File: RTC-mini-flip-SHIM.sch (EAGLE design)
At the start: 9 parts, among them IC1 DS3231/SO

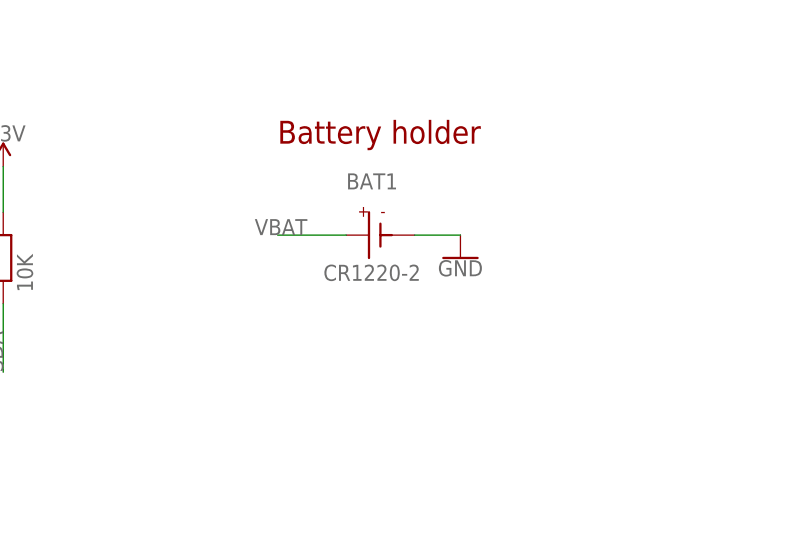
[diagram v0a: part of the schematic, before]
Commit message: Added battery connector. Generated CAM.
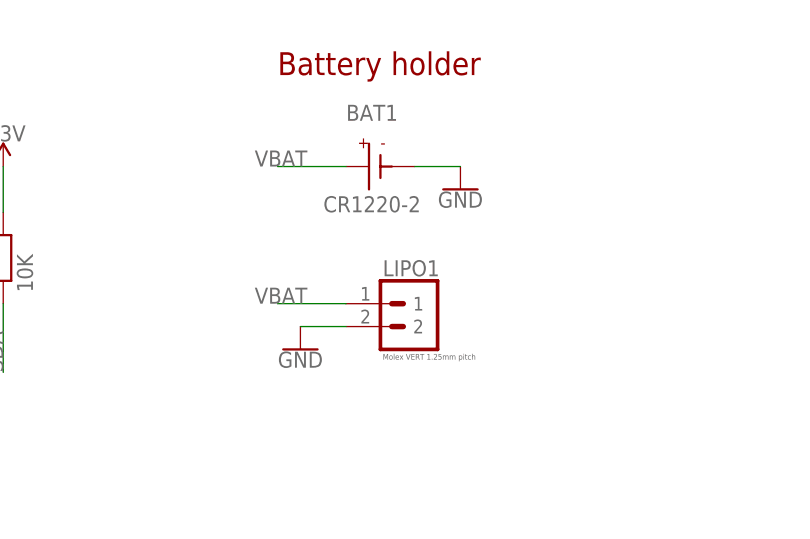
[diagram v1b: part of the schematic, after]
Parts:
- added LIPO1: Molex VERT 1.25mm pitch, PiB_connectors:1X02_MOLEX_0530470210_VERT-MALE_PITCH-1.25MM
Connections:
- net GND: now also LIPO1.2
- net VBAT: now also LIPO1.1
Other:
- moved on the sheet: BAT1
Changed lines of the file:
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@@
 <layer number="154" name="FabDoc2" color="2" fill="1" visible="no" active="no"/>
 <layer number="155" name="FabDoc3" color="7" fill="15" visible="no" active="no"/>
+<layer number="160" name="tMountFaceplate" color="7" fill="1" visible="yes" active="yes"/>
+<layer number="161" name="bMountFaceplate" color="7" fill="1" visible="yes" active="yes"/>
+<layer number="162" name="tCopperArt" color="7" fill="1" visible="yes" active="yes"/>
+<layer number="163" name="bCopperArt" color="7" fill="1" visible="yes" active="yes"/>
+<layer number="164" name="tRubout" color="7" fill="1" visible="yes" active="yes"/>
+<layer number="165" name="bRubout" color="7" fill="1" visible="yes" active="yes"/>
+<layer number="167" name="Fiducials" color="7" fill="1" visible="yes" active="yes"/>
+<layer number="169" name="internal" color="7" fill="1" visible="yes" active="yes"/>
 <layer number="199" name="Contour" color="7" fill="1" visible="no" active="yes"/>
 <layer number="200" name="200bmp" color="1" fill="10" visible="no" active="yes"/>
@@
 <part name="GND9" library="SparkFun-PowerSymbols" library_urn="urn:adsk.eagle:library:530" deviceset="GND" device=""/>
 <part name="LOGO1" library="_my_logos" deviceset="MFDECLOGO" device="_L_10MM"/>
+<part name="LIPO1" library="PiB_connectors" deviceset="1X02_MOLEX" device="_0530470210_VERT-MALE_PITCH-1.25MM" package3d_urn="urn:adsk.eagle:package:2973718/3" value="Molex VERT 1.25mm pitch"/>
+<part name="GND11" library="SparkFun-PowerSymbols" library_urn="urn:adsk.eagle:library:530" deviceset="GND" device=""/>
 </parts>
 <sheets>
@@
 <text x="152.4" y="124.46" size="2.54" layer="94">Caps and pullups</text>
 <text x="104.14" y="124.46" size="2.54" layer="94">Mini connector</text>
-<text x="210.82" y="116.84" size="2.54" layer="94">Battery holder</text>
+<text x="210.82" y="124.46" size="2.54" layer="94">Battery holder</text>
 </plain>
 <instances>
@@
 <attribute name="VALUE" x="101.6" y="93.726" size="1.778" layer="96" align="top-center"/>
 </instance>
-<instance part="BAT1" gate="G$1" x="220.98" y="106.68" smashed="yes">
-<attribute name="NAME" x="218.44" y="111.76" size="1.778" layer="96"/>
-<attribute name="VALUE" x="215.9" y="101.6" size="1.778" layer="96"/>
-</instance>
-<instance part="GND9" gate="1" x="231.14" y="104.14" smashed="yes">
-<attribute name="VALUE" x="231.14" y="103.886" size="1.778" layer="96" align="top-center"/>
+<instance part="BAT1" gate="G$1" x="220.98" y="114.3" smashed="yes">
+<attribute name="NAME" x="218.44" y="119.38" size="1.778" layer="96"/>
+<attribute name="VALUE" x="215.9" y="109.22" size="1.778" layer="96"/>
+</instance>
+<instance part="GND9" gate="1" x="231.14" y="111.76" smashed="yes">
+<attribute name="VALUE" x="231.14" y="111.506" size="1.778" layer="96" align="top-center"/>
 </instance>
 <instance part="LOGO1" gate="G$1" x="134.62" y="2.54" smashed="yes"/>
+<instance part="LIPO1" gate="G$1" x="226.06" y="99.06" smashed="yes" rot="MR0">
+<attribute name="VALUE" x="222.504" y="93.472" size="0.635" layer="96" font="vector" ratio="10" rot="MR0" align="top-right"/>
+<attribute name="NAME" x="222.504" y="102.108" size="1.778" layer="95" ratio="10" rot="MR0" align="bottom-right"/>
+</instance>
+<instance part="GND11" gate="1" x="213.36" y="93.98" smashed="yes">
+<attribute name="VALUE" x="213.36" y="93.726" size="1.778" layer="96" align="top-center"/>
+</instance>
 </instances>
 <busses>
@@
 <segment>
 <pinref part="BAT1" gate="G$1" pin="BAT+"/>
-<wire x1="218.44" y1="106.68" x2="210.82" y2="106.68" width="0.1524" layer="91"/>
-<label x="208.28" y="106.68" size="1.778" layer="95"/>
+<wire x1="218.44" y1="114.3" x2="210.82" y2="114.3" width="0.1524" layer="91"/>
+<label x="208.28" y="114.3" size="1.778" layer="95"/>
+</segment>
+<segment>
+<pinref part="LIPO1" gate="G$1" pin="1"/>
+<wire x1="218.44" y1="99.06" x2="210.82" y2="99.06" width="0.1524" layer="91"/>
+<label x="208.28" y="99.06" size="1.778" layer="95"/>
 </segment>
 </net>
@@
 <segment>
 <pinref part="BAT1" gate="G$1" pin="BAT-"/>
-<wire x1="226.06" y1="106.68" x2="231.14" y2="106.68" width="0.1524" layer="91"/>
+<wire x1="226.06" y1="114.3" x2="231.14" y2="114.3" width="0.1524" layer="91"/>
 <pinref part="GND9" gate="1" pin="GND"/>
 </segment>
-</net>
+<segment>
+<pinref part="LIPO1" gate="G$1" pin="2"/>
+<wire x1="218.44" y1="96.52" x2="213.36" y2="96.52" width="0.1524" layer="91"/>
+<pinref part="GND11" gate="1" pin="GND"/>
+</segment>
+</net>

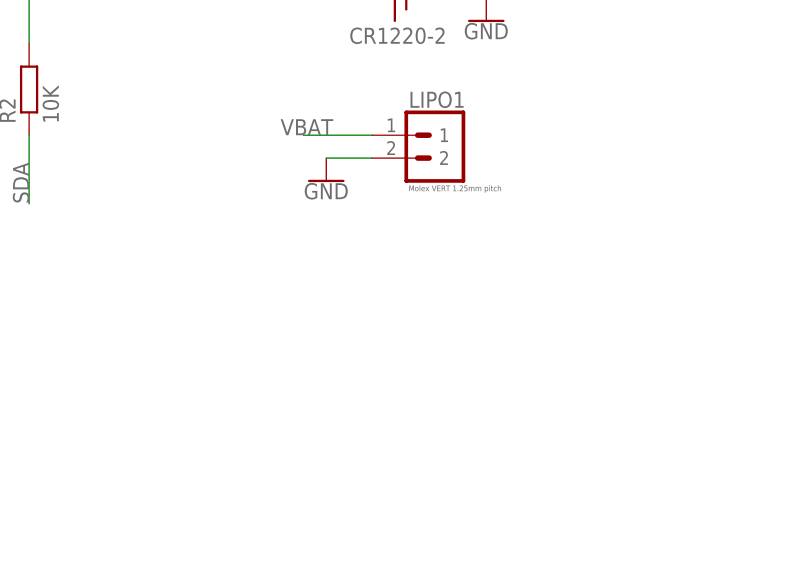
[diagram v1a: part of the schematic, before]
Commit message: Add battery connector to the front of mini SHIM too. Generate new CAM.
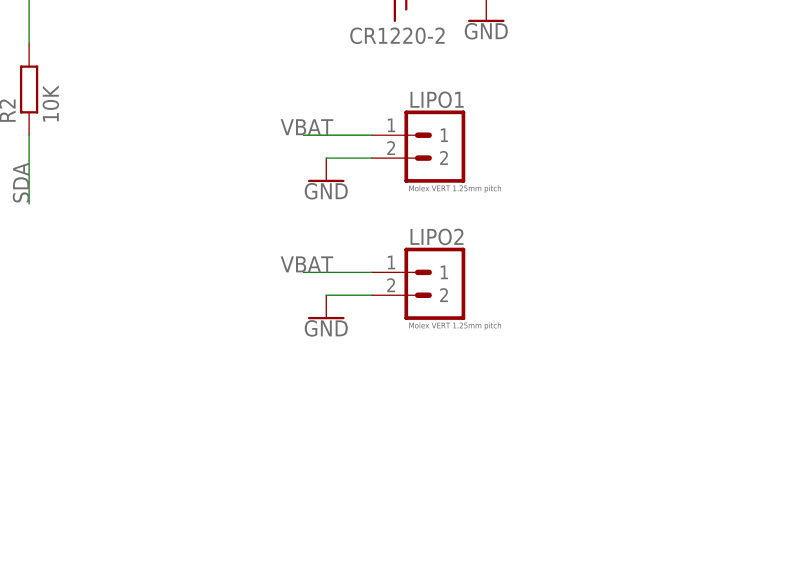
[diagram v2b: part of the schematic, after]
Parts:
- added LIPO2: Molex VERT 1.25mm pitch, PiB_connectors:1X02_MOLEX_0530470210_VERT-MALE_PITCH-1.25MM
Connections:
- net GND: now also LIPO2.2
- net VBAT: now also LIPO2.1
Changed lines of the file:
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@@
 <part name="LIPO1" library="PiB_connectors" deviceset="1X02_MOLEX" device="_0530470210_VERT-MALE_PITCH-1.25MM" package3d_urn="urn:adsk.eagle:package:2973718/3" value="Molex VERT 1.25mm pitch"/>
 <part name="GND11" library="SparkFun-PowerSymbols" library_urn="urn:adsk.eagle:library:530" deviceset="GND" device=""/>
+<part name="LIPO2" library="PiB_connectors" deviceset="1X02_MOLEX" device="_0530470210_VERT-MALE_PITCH-1.25MM" package3d_urn="urn:adsk.eagle:package:2973718/3" value="Molex VERT 1.25mm pitch"/>
+<part name="GND6" library="SparkFun-PowerSymbols" library_urn="urn:adsk.eagle:library:530" deviceset="GND" device=""/>
 </parts>
 <sheets>
@@
 <attribute name="VALUE" x="213.36" y="93.726" size="1.778" layer="96" align="top-center"/>
 </instance>
+<instance part="LIPO2" gate="G$1" x="226.06" y="83.82" smashed="yes" rot="MR0">
+<attribute name="VALUE" x="222.504" y="78.232" size="0.635" layer="96" font="vector" ratio="10" rot="MR0" align="top-right"/>
+<attribute name="NAME" x="222.504" y="86.868" size="1.778" layer="95" ratio="10" rot="MR0" align="bottom-right"/>
+</instance>
+<instance part="GND6" gate="1" x="213.36" y="78.74" smashed="yes">
+<attribute name="VALUE" x="213.36" y="78.486" size="1.778" layer="96" align="top-center"/>
+</instance>
 </instances>
 <busses>
@@
 <wire x1="218.44" y1="99.06" x2="210.82" y2="99.06" width="0.1524" layer="91"/>
 <label x="208.28" y="99.06" size="1.778" layer="95"/>
+</segment>
+<segment>
+<pinref part="LIPO2" gate="G$1" pin="1"/>
+<wire x1="218.44" y1="83.82" x2="210.82" y2="83.82" width="0.1524" layer="91"/>
+<label x="208.28" y="83.82" size="1.778" layer="95"/>
 </segment>
 </net>
@@
 <pinref part="GND11" gate="1" pin="GND"/>
 </segment>
-</net>
+<segment>
+<pinref part="LIPO2" gate="G$1" pin="2"/>
+<wire x1="218.44" y1="81.28" x2="213.36" y2="81.28" width="0.1524" layer="91"/>
+<pinref part="GND6" gate="1" pin="GND"/>
+</segment>
+</net>

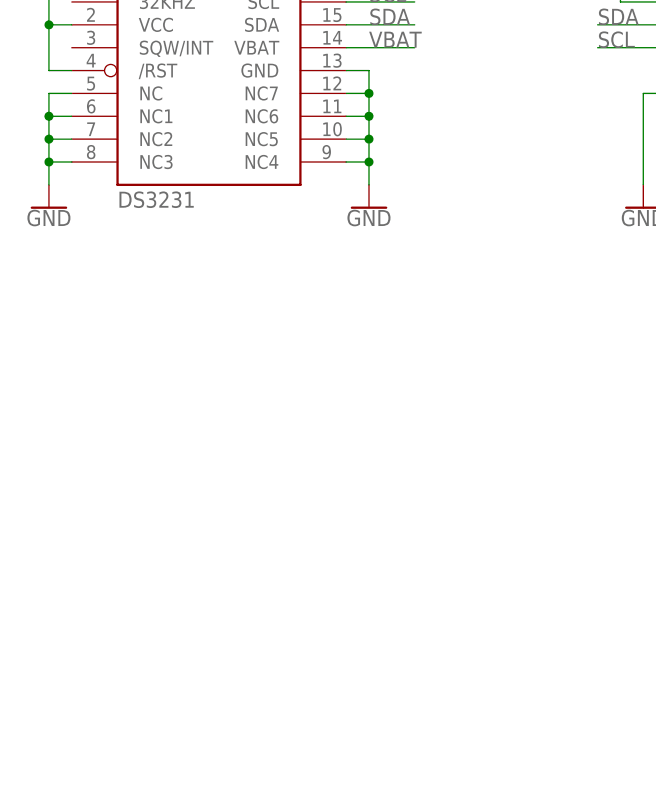
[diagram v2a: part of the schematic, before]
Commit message: Moved some stuff around. Add second footprint. Moved battery away from center for better flipability.
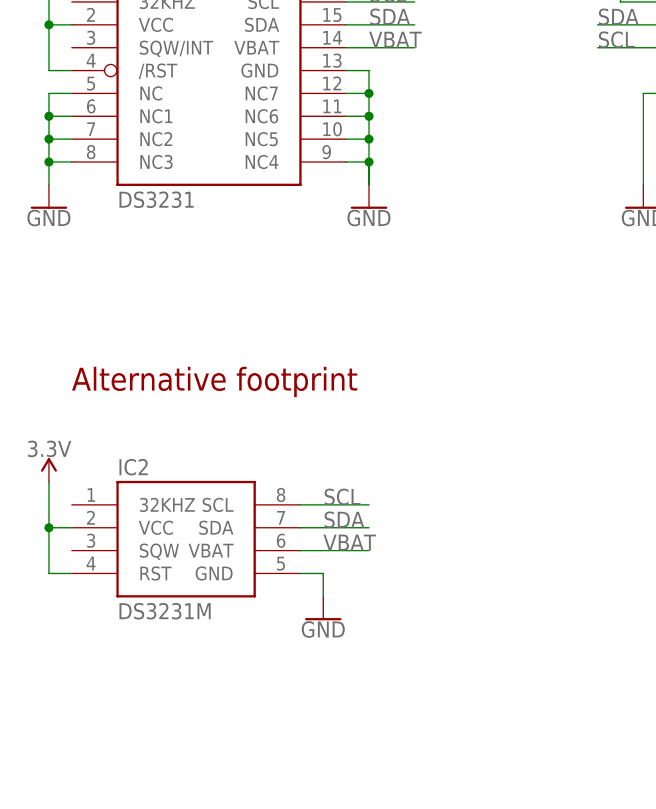
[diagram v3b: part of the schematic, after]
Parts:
- added IC2: DS3231M, SparkFun-Clocks:DS3231M
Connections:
- net 3.3V: now also IC2.RST, IC2.VCC
- net GND: now also IC2.GND
- net SCL: now also IC2.SCL
- net SDA: now also IC2.SDA
- net VBAT: now also IC2.VBAT
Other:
- note added: "Alternative footprint"
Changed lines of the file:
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@@
 <part name="LIPO2" library="PiB_connectors" deviceset="1X02_MOLEX" device="_0530470210_VERT-MALE_PITCH-1.25MM" package3d_urn="urn:adsk.eagle:package:2973718/3" value="Molex VERT 1.25mm pitch"/>
 <part name="GND6" library="SparkFun-PowerSymbols" library_urn="urn:adsk.eagle:library:530" deviceset="GND" device=""/>
+<part name="IC2" library="SparkFun-Clocks" library_urn="urn:adsk.eagle:library:511" deviceset="DS3231M" device="" package3d_urn="urn:adsk.eagle:package:37530/1"/>
+<part name="SUPPLY7" library="SparkFun-PowerSymbols" library_urn="urn:adsk.eagle:library:530" deviceset="3.3V" device=""/>
+<part name="GND7" library="SparkFun-PowerSymbols" library_urn="urn:adsk.eagle:library:530" deviceset="GND" device=""/>
 </parts>
 <sheets>
@@
 <text x="104.14" y="124.46" size="2.54" layer="94">Mini connector</text>
 <text x="210.82" y="124.46" size="2.54" layer="94">Battery holder</text>
+<text x="38.1" y="73.66" size="2.54" layer="94">Alternative footprint</text>
 </plain>
 <instances>
@@
 <attribute name="VALUE" x="213.36" y="78.486" size="1.778" layer="96" align="top-center"/>
 </instance>
+<instance part="IC2" gate="G$1" x="50.8" y="55.88" smashed="yes">
+<attribute name="NAME" x="43.18" y="64.262" size="1.778" layer="95" ratio="10"/>
+<attribute name="VALUE" x="43.18" y="48.26" size="1.778" layer="96" ratio="10"/>
+</instance>
+<instance part="SUPPLY7" gate="G$1" x="35.56" y="63.5" smashed="yes">
+<attribute name="VALUE" x="35.56" y="66.294" size="1.778" layer="96" align="bottom-center"/>
+</instance>
+<instance part="GND7" gate="1" x="66.04" y="48.26" smashed="yes">
+<attribute name="VALUE" x="66.04" y="48.006" size="1.778" layer="96" align="top-center"/>
+</instance>
 </instances>
 <busses>
@@
 <label x="208.28" y="83.82" size="1.778" layer="95"/>
 </segment>
+<segment>
+<pinref part="IC2" gate="G$1" pin="VBAT"/>
+<wire x1="63.5" y1="55.88" x2="71.12" y2="55.88" width="0.1524" layer="91"/>
+<label x="66.04" y="55.88" size="1.778" layer="95"/>
+</segment>
 </net>
 <net name="SCL" class="0">
@@
 <label x="96.52" y="111.76" size="1.778" layer="95"/>
 </segment>
+<segment>
+<pinref part="IC2" gate="G$1" pin="SCL"/>
+<wire x1="63.5" y1="60.96" x2="71.12" y2="60.96" width="0.1524" layer="91"/>
+<label x="66.04" y="60.96" size="1.778" layer="95"/>
+</segment>
 </net>
 <net name="SDA" class="0">
@@
 <wire x1="104.14" y1="114.3" x2="96.52" y2="114.3" width="0.1524" layer="91"/>
 <label x="96.52" y="114.3" size="1.778" layer="95"/>
+</segment>
+<segment>
+<pinref part="IC2" gate="G$1" pin="SDA"/>
+<wire x1="63.5" y1="58.42" x2="71.12" y2="58.42" width="0.1524" layer="91"/>
+<label x="66.04" y="58.42" size="1.778" layer="95"/>
 </segment>
 </net>
@@
 <wire x1="99.06" y1="116.84" x2="99.06" y2="119.38" width="0.1524" layer="91"/>
 <pinref part="SUPPLY6" gate="G$1" pin="3.3V"/>
+</segment>
+<segment>
+<pinref part="IC2" gate="G$1" pin="RST"/>
+<wire x1="38.1" y1="53.34" x2="35.56" y2="53.34" width="0.1524" layer="91"/>
+<wire x1="35.56" y1="53.34" x2="35.56" y2="58.42" width="0.1524" layer="91"/>
+<pinref part="IC2" gate="G$1" pin="VCC"/>
+<wire x1="35.56" y1="58.42" x2="35.56" y2="63.5" width="0.1524" layer="91"/>
+<wire x1="38.1" y1="58.42" x2="35.56" y2="58.42" width="0.1524" layer="91"/>
+<junction x="35.56" y="58.42"/>
+<pinref part="SUPPLY7" gate="G$1" pin="3.3V"/>
 </segment>
 </net>
@@
 <wire x1="68.58" y1="106.68" x2="71.12" y2="106.68" width="0.1524" layer="91"/>
 <junction x="71.12" y="106.68"/>
+<wire x1="71.12" y1="99.06" x2="71.12" y2="96.52" width="0.1524" layer="91"/>
 </segment>
 <segment>
@@
 <pinref part="GND6" gate="1" pin="GND"/>
 </segment>
-</net>
+<segment>
+<pinref part="IC2" gate="G$1" pin="GND"/>
+<wire x1="63.5" y1="53.34" x2="66.04" y2="53.34" width="0.1524" layer="91"/>
+<wire x1="66.04" y1="53.34" x2="66.04" y2="50.8" width="0.1524" layer="91"/>
+<pinref part="GND7" gate="1" pin="GND"/>
+</segment>
+</net>

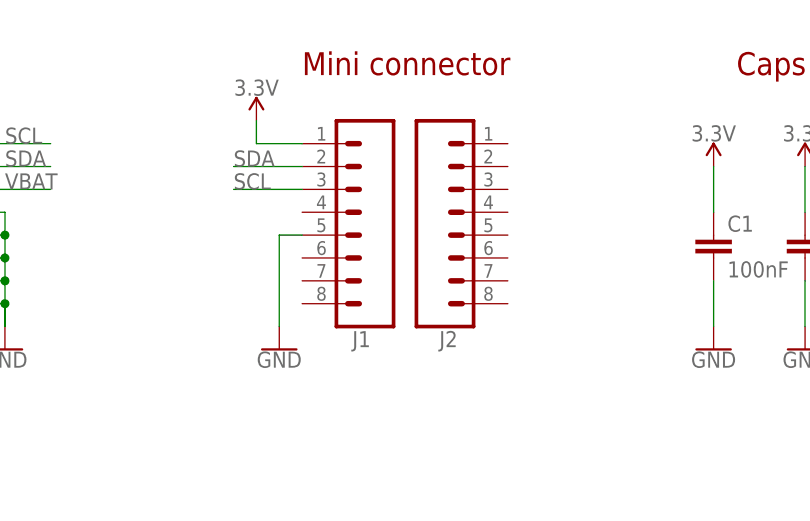
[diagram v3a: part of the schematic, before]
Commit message: Changed mini SHIM layout. Traced mini SHIM.
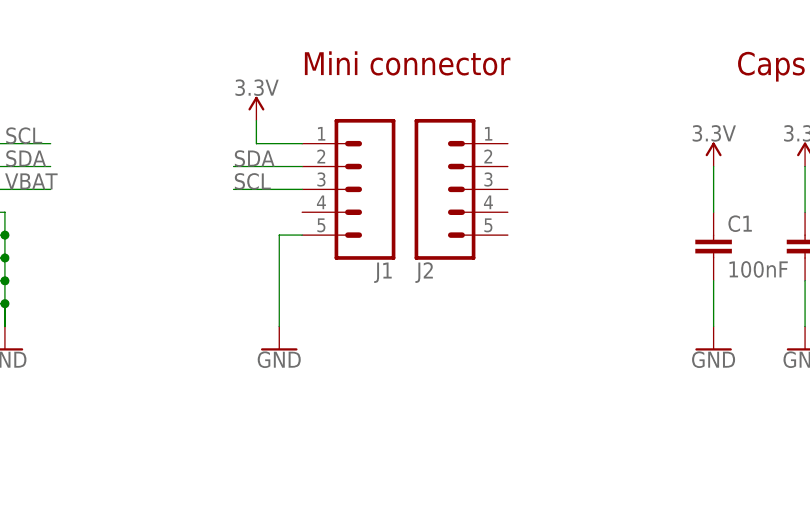
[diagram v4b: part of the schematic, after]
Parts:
- J1, J2: device SparkFun-Connectors:CONN_08LOCK_NO_SILK -> SparkFun-Connectors:CONN_05LOCK
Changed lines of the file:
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@@
 <part name="SUPPLY4" library="SparkFun-PowerSymbols" library_urn="urn:adsk.eagle:library:530" deviceset="3.3V" device=""/>
 <part name="SUPPLY5" library="SparkFun-PowerSymbols" library_urn="urn:adsk.eagle:library:530" deviceset="3.3V" device=""/>
-<part name="J1" library="SparkFun-Connectors" library_urn="urn:adsk.eagle:library:513" deviceset="CONN_08" device="LOCK_NO_SILK" package3d_urn="urn:adsk.eagle:package:38147/1"/>
-<part name="J2" library="SparkFun-Connectors" library_urn="urn:adsk.eagle:library:513" deviceset="CONN_08" device="LOCK_NO_SILK" package3d_urn="urn:adsk.eagle:package:38147/1"/>
+<part name="J1" library="SparkFun-Connectors" library_urn="urn:adsk.eagle:library:513" deviceset="CONN_05" device="LOCK" package3d_urn="urn:adsk.eagle:package:38105/1"/>
+<part name="J2" library="SparkFun-Connectors" library_urn="urn:adsk.eagle:library:513" deviceset="CONN_05" device="LOCK" package3d_urn="urn:adsk.eagle:package:38105/1"/>
 <part name="SUPPLY6" library="SparkFun-PowerSymbols" library_urn="urn:adsk.eagle:library:530" deviceset="3.3V" device=""/>
 <part name="GND5" library="SparkFun-PowerSymbols" library_urn="urn:adsk.eagle:library:530" deviceset="GND" device=""/>
@@
 <attribute name="VALUE" x="180.34" y="117.094" size="1.778" layer="96" align="bottom-center"/>
 </instance>
-<instance part="J1" gate="G$1" x="109.22" y="109.22" smashed="yes" rot="R180">
-<attribute name="VALUE" x="109.22" y="108.966" size="1.778" layer="96" font="vector" rot="R180"/>
-<attribute name="NAME" x="111.76" y="96.012" size="1.778" layer="95" rot="R180"/>
+<instance part="J1" gate="G$1" x="111.76" y="111.76" smashed="yes" rot="R180">
+<attribute name="VALUE" x="111.76" y="111.506" size="1.778" layer="96" font="vector" rot="R180"/>
+<attribute name="NAME" x="114.3" y="103.632" size="1.778" layer="95" rot="R180"/>
 </instance>
-<instance part="J2" gate="G$1" x="121.92" y="109.22" smashed="yes" rot="MR180">
-<attribute name="VALUE" x="121.92" y="108.966" size="1.778" layer="96" font="vector" rot="MR180"/>
-<attribute name="NAME" x="119.38" y="96.012" size="1.778" layer="95" rot="MR180"/>
+<instance part="J2" gate="G$1" x="119.38" y="111.76" smashed="yes" rot="MR180">
+<attribute name="VALUE" x="119.38" y="111.506" size="1.778" layer="96" font="vector" rot="MR180"/>
+<attribute name="NAME" x="116.84" y="103.632" size="1.778" layer="95" rot="MR180"/>
 </instance>
 <instance part="SUPPLY6" gate="G$1" x="99.06" y="119.38" smashed="yes">
